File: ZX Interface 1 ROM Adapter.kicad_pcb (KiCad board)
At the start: 2 copper layers, 31 x 44 mm, 4 parts, among them J1 Conn_01x08_Socket, J2 24DIL Socket, J3 Conn_01x16, J4 Conn_01x16

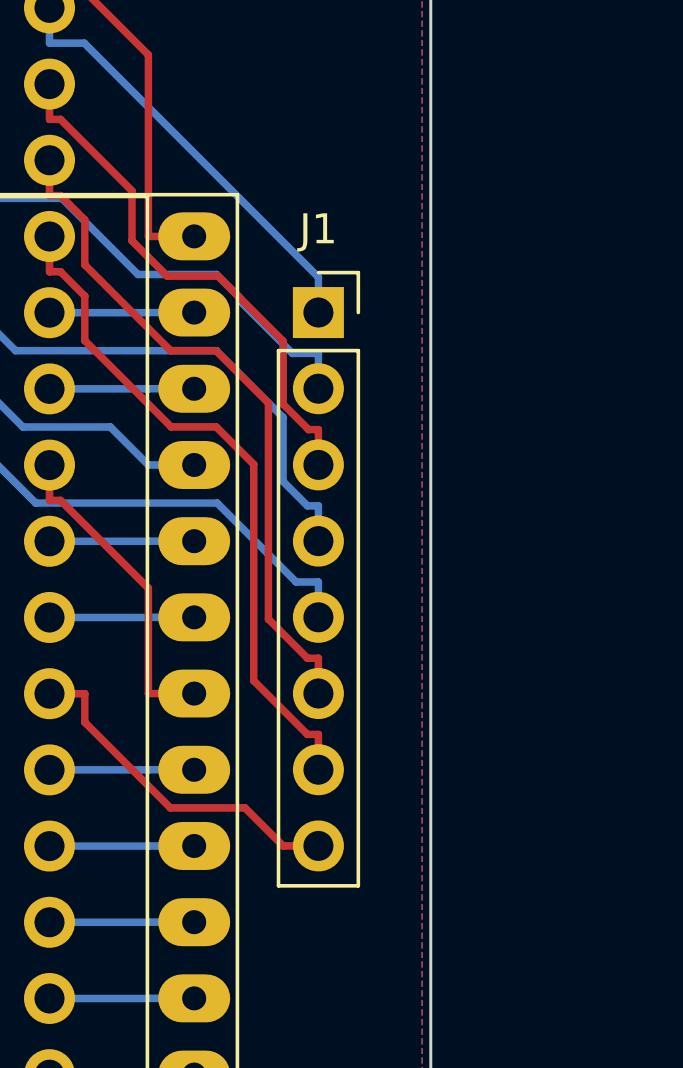
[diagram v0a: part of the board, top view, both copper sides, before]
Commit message: Updated to use 8 Pin Right Angled Single-In-Line Connector
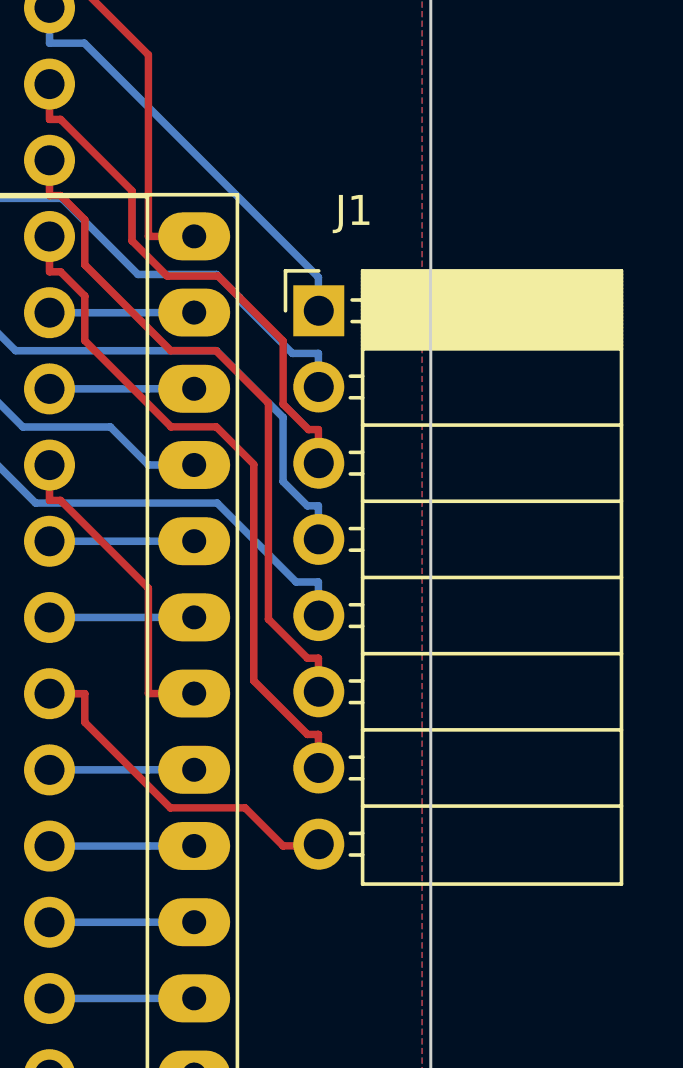
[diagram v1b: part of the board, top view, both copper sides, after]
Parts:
- J1: footprint Connector_PinSocket_2.54mm:PinSocket_1x08_P2.54mm_Vertical -> Library:PinSocket_1x08_P2.54mm_HorizontalR
- moved J1 10.2 mm to (113.4, 84.8)

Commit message: Add files via upload
Updated to Kicad 9. Added ibom. Restructured folders.
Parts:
- J1: footprint Library:PinSocket_1x08_P2.54mm_HorizontalR -> Mod:PinSocket_1x08_P2.54mm_HorizontalR
- J2: footprint Package_DIP:DIP-24_W15.24mm_Socket_LongPads -> Mod:DIP-24_W15.24mm_Socket_LongPads
- J3, J4: footprint Connector_PinHeader_2.54mm:PinHeader_1x16_P2.54mm_Vertical -> Mod:PinHeader_1x16_P2.54mm_Vertical
